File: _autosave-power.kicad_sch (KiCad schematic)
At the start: 16 parts, among them U1 HT7533-1, U2 TLV62569DBV

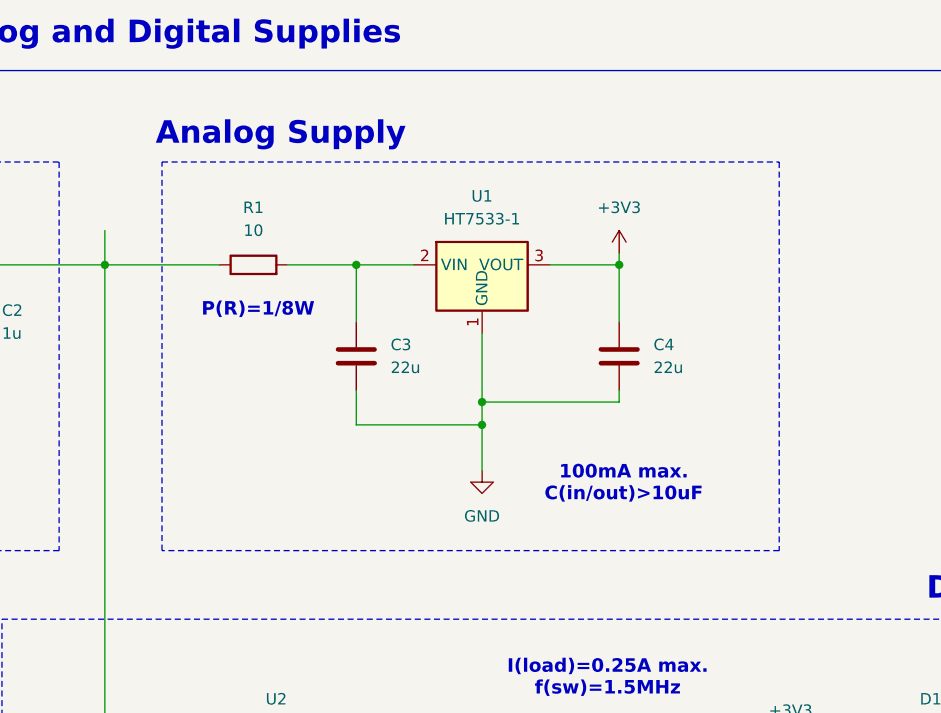
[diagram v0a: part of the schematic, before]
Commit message: Added notes to next lesson: Power Supply Design
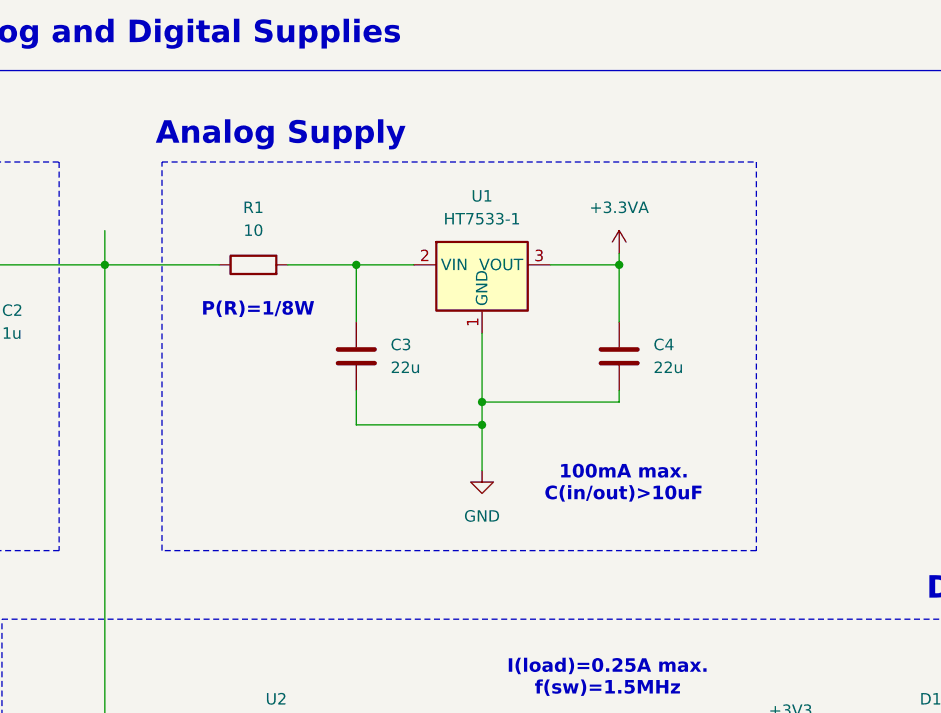
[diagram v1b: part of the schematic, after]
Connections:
- net +3V3: no longer C4.1, U1.3 (VOUT)
- new net +3.3VA: C4.1, U1.3 (VOUT)
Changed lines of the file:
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@@
 	(rectangle
 		(start 85.09 50.8)
-		(end 153.67 93.98)
+		(end 151.13 93.98)
 		(stroke
 			(width 0)
@@
 	)
 	(symbol
+		(lib_id "Device:C")
+		(at 38.1 68.58 0)
+		(unit 1)
+		(exclude_from_sim no)
+		(in_bom yes)
+		(on_board yes)
+		(dnp no)
+		(fields_autoplaced yes)
+		(property "Reference" "C1"
+			(at 41.91 67.3099 0)
+			(effects
+				(font
+					(size 1.27 1.27)
+				)
+				(justify left)
+			)
+		)
+		(property "Value" "1u"
+			(at 41.91 69.8499 0)
+			(effects
+				(font
+					(size 1.27 1.27)
+				)
+				(justify left)
+			)
+		)
+		(property "Footprint" ""
+			(at 39.0652 72.39 0)
+			(effects
+				(font
+					(size 1.27 1.27)
+				)
+				(hide yes)
+			)
+		)
+		(property "Datasheet" "~"
+			(at 38.1 68.58 0)
+			(effects
+				(font
+					(size 1.27 1.27)
+				)
+				(hide yes)
+			)
+		)
+		(property "Description" "Unpolarized capacitor"
+			(at 38.1 68.58 0)
+			(effects
+				(font
+					(size 1.27 1.27)
+				)
+				(hide yes)
+			)
+		)
+		(pin "1"
+		)
+		(pin "2"
+		)
+		(instances
+			(project ""
+				(path "/eba96202-8ea2-41d9-8d7a-700a4166585a/9e6a3319-b22e-494d-bd14-b1d6263414e0"
+					(reference "C1")
+					(unit 1)
+				)
+			)
+		)
+	)
+	(symbol
+		(lib_id "Device:R")
+		(at 147.32 124.46 0)
+		(unit 1)
+		(exclude_from_sim no)
+		(in_bom yes)
+		(on_board yes)
+		(dnp no)
+		(fields_autoplaced yes)
+		(property "Reference" "R2"
+			(at 149.86 123.1899 0)
+			(effects
+				(font
+					(size 1.27 1.27)
+				)
+				(justify left)
+			)
+		)
+		(property "Value" "100k"
+			(at 149.86 125.7299 0)
+			(effects
+				(font
+					(size 1.27 1.27)
+				)
+				(justify left)
+			)
+		)
+		(property "Footprint" ""
+			(at 145.542 124.46 90)
+			(effects
+				(font
+					(size 1.27 1.27)
+				)
+				(hide yes)
+			)
+		)
+		(property "Datasheet" "~"
+			(at 147.32 124.46 0)
+			(effects
+				(font
+					(size 1.27 1.27)
+				)
+				(hide yes)
+			)
+		)
+		(property "Description" "Resistor"
+			(at 147.32 124.46 0)
+			(effects
+				(font
+					(size 1.27 1.27)
+				)
+				(hide yes)
+			)
+		)
+		(pin "2"
+		)
+		(pin "1"
+		)
+		(instances
+			(project ""
+				(path "/eba96202-8ea2-41d9-8d7a-700a4166585a/9e6a3319-b22e-494d-bd14-b1d6263414e0"
+					(reference "R2")
+					(unit 1)
+				)
+			)
+		)
+	)
+	(symbol
 		(lib_id "power:+3V3")
+		(at 154.94 116.84 0)
+		(unit 1)
+		(exclude_from_sim no)
+		(in_bom yes)
+		(on_board yes)
+		(dnp no)
+		(fields_autoplaced yes)
+		(property "Reference" "#PWR08"
+			(at 154.94 120.65 0)
+			(effects
+				(font
+					(size 1.27 1.27)
+				)
+				(hide yes)
+			)
+		)
+		(property "Value" "+3V3"
+			(at 154.94 111.76 0)
+			(effects
+				(font
+					(size 1.27 1.27)
+				)
+			)
+		)
+		(property "Footprint" ""
+			(at 154.94 116.84 0)
+			(effects
+				(font
+					(size 1.27 1.27)
+				)
+				(hide yes)
+			)
+		)
+		(property "Datasheet" ""
+			(at 154.94 116.84 0)
+			(effects
+				(font
+					(size 1.27 1.27)
+				)
+				(hide yes)
+			)
+		)
+		(property "Description" "Power symbol creates a global label with name \"+3V3\""
+			(at 154.94 116.84 0)
+			(effects
+				(font
+					(size 1.27 1.27)
+				)
+				(hide yes)
+			)
+		)
+		(pin "1"
+		)
+		(instances
+			(project ""
+				(path "/eba96202-8ea2-41d9-8d7a-700a4166585a/9e6a3319-b22e-494d-bd14-b1d6263414e0"
+					(reference "#PWR08")
+					(unit 1)
+				)
+			)
+		)
+	)
+	(symbol
+		(lib_id "power:+3.3VA")
 		(at 135.89 60.96 0)
 		(unit 1)
@@
 			)
 		)
-		(property "Value" "+3V3"
+		(property "Value" "+3.3VA"
 			(at 135.89 55.88 0)
 			(effects
@@
 			)
 		)
-		(property "Description" "Power symbol creates a global label with name \"+3V3\""
+		(property "Description" "Power symbol creates a global label with name \"+3.3VA\""
 			(at 135.89 60.96 0)
 			(effects
@@
 					(unit 1)
 				)
-			)
-		)
-	)
-	(symbol
-		(lib_id "Device:C")
-		(at 38.1 68.58 0)
-		(unit 1)
-		(exclude_from_sim no)
-		(in_bom yes)
-		(on_board yes)
-		(dnp no)
-		(fields_autoplaced yes)
-		(property "Reference" "C1"
-			(at 41.91 67.3099 0)
-			(effects
-				(font
-					(size 1.27 1.27)
-				)
-				(justify left)
-			)
-		)
-		(property "Value" "1u"
-			(at 41.91 69.8499 0)
-			(effects
-				(font
-					(size 1.27 1.27)
-				)
-				(justify left)
-			)
-		)
-		(property "Footprint" ""
-			(at 39.0652 72.39 0)
-			(effects
-				(font
-					(size 1.27 1.27)
-				)
-				(hide yes)
-			)
-		)
-		(property "Datasheet" "~"
-			(at 38.1 68.58 0)
-			(effects
-				(font
-					(size 1.27 1.27)
-				)
-				(hide yes)
-			)
-		)
-		(property "Description" "Unpolarized capacitor"
-			(at 38.1 68.58 0)
-			(effects
-				(font
-					(size 1.27 1.27)
-				)
-				(hide yes)
-			)
-		)
-		(pin "1"
-		)
-		(pin "2"
-		)
-		(instances
-			(project ""
-				(path "/eba96202-8ea2-41d9-8d7a-700a4166585a/9e6a3319-b22e-494d-bd14-b1d6263414e0"
-					(reference "C1")
-					(unit 1)
-				)
-			)
-		)
-	)
-	(symbol
-		(lib_id "Device:R")
-		(at 147.32 124.46 0)
-		(unit 1)
-		(exclude_from_sim no)
-		(in_bom yes)
-		(on_board yes)
-		(dnp no)
-		(fields_autoplaced yes)
-		(property "Reference" "R2"
-			(at 149.86 123.1899 0)
-			(effects
-				(font
-					(size 1.27 1.27)
-				)
-				(justify left)
-			)
-		)
-		(property "Value" "100k"
-			(at 149.86 125.7299 0)
-			(effects
-				(font
-					(size 1.27 1.27)
-				)
-				(justify left)
-			)
-		)
-		(property "Footprint" ""
-			(at 145.542 124.46 90)
-			(effects
-				(font
-					(size 1.27 1.27)
-				)
-				(hide yes)
-			)
-		)
-		(property "Datasheet" "~"
-			(at 147.32 124.46 0)
-			(effects
-				(font
-					(size 1.27 1.27)
-				)
-				(hide yes)
-			)
-		)
-		(property "Description" "Resistor"
-			(at 147.32 124.46 0)
-			(effects
-				(font
-					(size 1.27 1.27)
-				)
-				(hide yes)
-			)
-		)
-		(pin "2"
-		)
-		(pin "1"
-		)
-		(instances
-			(project ""
-				(path "/eba96202-8ea2-41d9-8d7a-700a4166585a/9e6a3319-b22e-494d-bd14-b1d6263414e0"
-					(reference "R2")
-					(unit 1)
-				)
-			)
-		)
-	)
-	(symbol
-		(lib_id "power:+3V3")
-		(at 154.94 116.84 0)
-		(unit 1)
-		(exclude_from_sim no)
-		(in_bom yes)
-		(on_board yes)
-		(dnp no)
-		(fields_autoplaced yes)
-		(property "Reference" "#PWR08"
-			(at 154.94 120.65 0)
-			(effects
-				(font
-					(size 1.27 1.27)
-				)
-				(hide yes)
-			)
-		)
-		(property "Value" "+3V3"
-			(at 154.94 111.76 0)
-			(effects
-				(font
-					(size 1.27 1.27)
-				)
-			)
-		)
-		(property "Footprint" ""
-			(at 154.94 116.84 0)
-			(effects
-				(font
-					(size 1.27 1.27)
-				)
-				(hide yes)
-			)
-		)
-		(property "Datasheet" ""
-			(at 154.94 116.84 0)
-			(effects
-				(font
-					(size 1.27 1.27)
-				)
-				(hide yes)
-			)
-		)
-		(property "Description" "Power symbol creates a global label with name \"+3V3\""
-			(at 154.94 116.84 0)
-			(effects
-				(font
-					(size 1.27 1.27)
-				)
-				(hide yes)
-			)
-		)
-		(pin "1"
-		)
-		(instances
-			(project ""
-				(path "/eba96202-8ea2-41d9-8d7a-700a4166585a/9e6a3319-b22e-494d-bd14-b1d6263414e0"
-					(reference "#PWR08")
-					(unit 1)
-				)
